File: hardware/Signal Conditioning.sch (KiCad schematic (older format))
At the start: 16 parts, among them U2 LM2902N

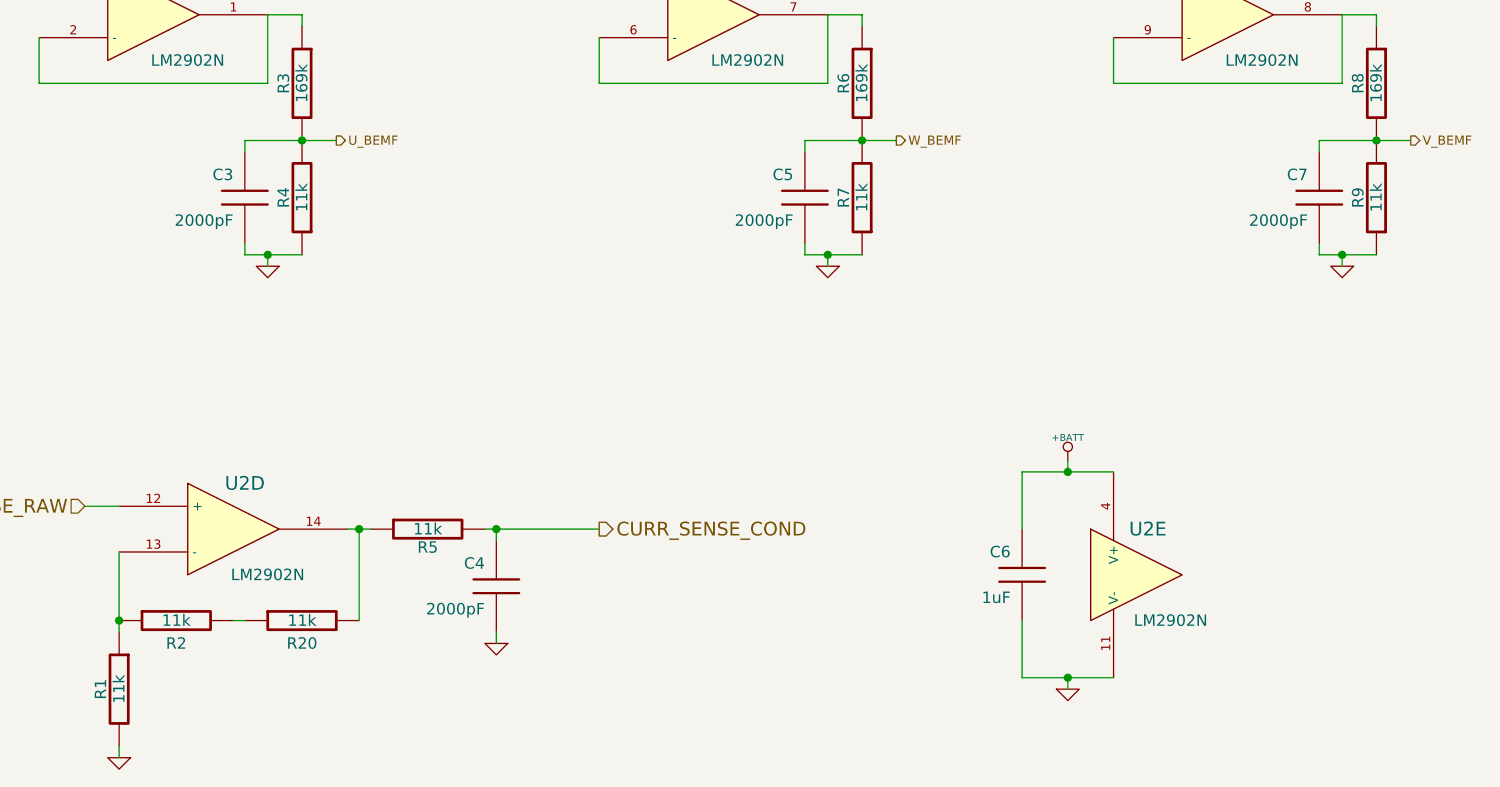
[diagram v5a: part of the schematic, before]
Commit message: Fixed item properties and generated a BOM.
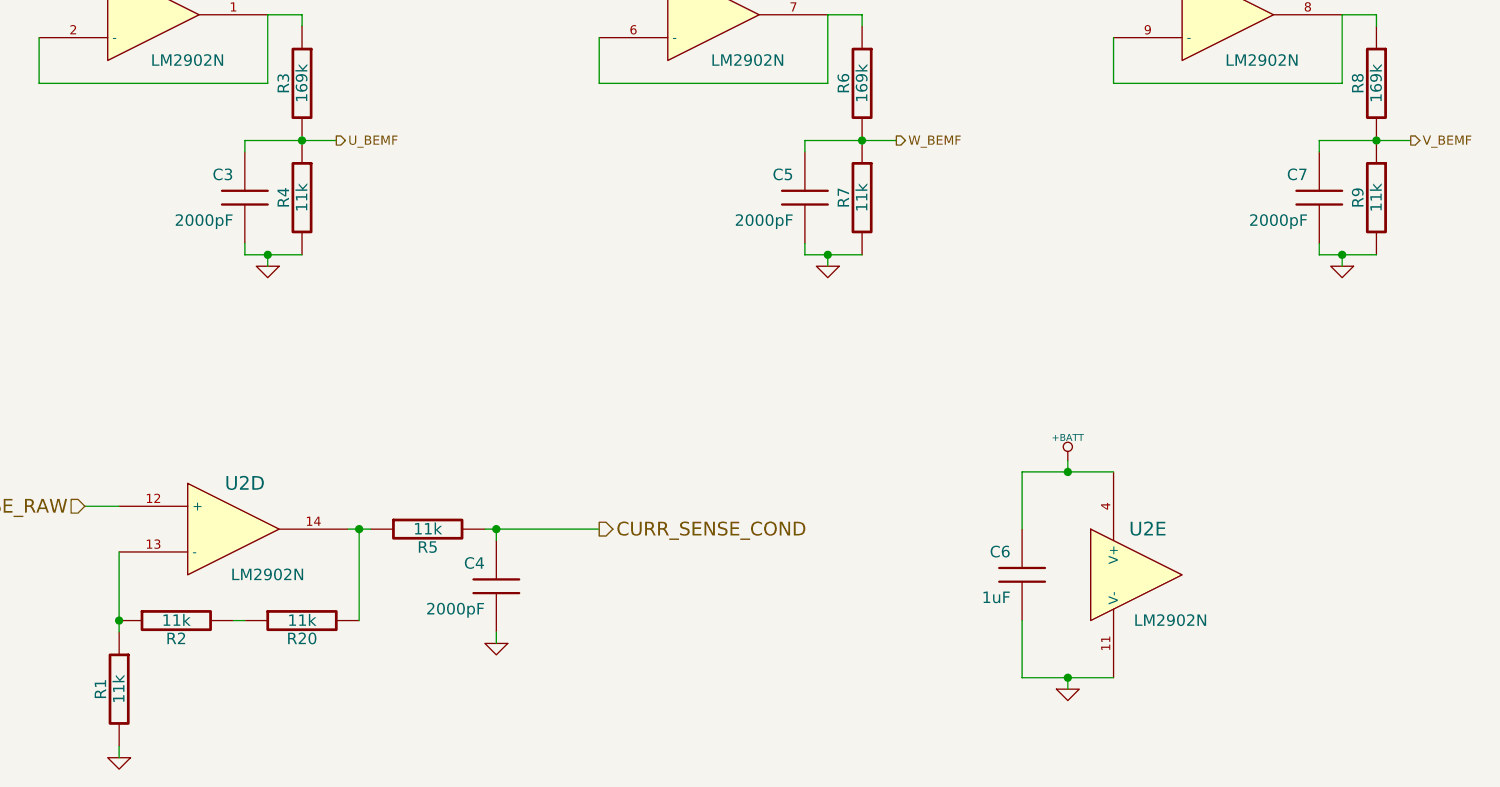
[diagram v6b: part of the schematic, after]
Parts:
- R1, R5: Digikey P/N 7.15KXBK-ND -> 11.0KXBK-ND; Mfg P/N MFR-25FBF52-7K15 -> MFR-25FBF52-11K; Mouser P/N 603-MFR-25FBF52-7K15 -> 603-MFR-25FBF52-11K
- R2, R20: Digikey P/N 169KXBK-ND -> 11.0KXBK-ND; Mfg P/N MFR-25FBF52-169K -> MFR-25FBF52-11K; Mouser P/N 603-MFR-25FBF52-169K -> 603-MFR-25FBF52-11K
- U2: Digikey P/N (none) -> LM2902NFS-ND; Mfg P/N (none) -> LM2902N; Mouser P/N (none) -> 512-LM2902N
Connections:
- net GND: now also R4.2, R7.2, R9.2; no longer R4.1, R7.1, R9.1
- net U_BEMF: now also R4.1; no longer R4.2
- net V_BEMF: now also R9.1; no longer R9.2
- net W_BEMF: now also R7.1; no longer R7.2
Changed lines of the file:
@@
-EESchema Schematic File Version 2  date Sun 14 Jun 2015 10:56:58 MST
+EESchema Schematic File Version 2  date Sun 14 Jun 2015 15:22:49 MST
 LIBS:power
 LIBS:device
@@
 Comment4 ""
 $EndDescr
+$Comp
+L R R5
+U 1 1 557DF4C5
+P 4350 4550
+F 0 "R5" V 4430 4550 50  0000 C CNN
+F 1 "11k" V 4350 4550 50  0000 C CNN
+F 4 "MFR-25FBF52-11K" V 4350 4550 60  0001 C CNN "Mfg P/N"
+F 5 "11.0KXBK-ND" V 4350 4550 60  0001 C CNN "Digikey P/N"
+F 6 "603-MFR-25FBF52-11K" V 4350 4550 60  0001 C CNN "Mouser P/N"
+	1    4350 4550
+	0    -1   1    0
+$EndComp
+$Comp
+L R R9
+U 1 1 557DF4AD
+P 8500 3100
+F 0 "R9" V 8580 3100 50  0000 C CNN
+F 1 "11k" V 8500 3100 50  0000 C CNN
+F 4 "MFR-25FBF52-11K" V 8500 3100 60  0001 C CNN "Mfg P/N"
+F 5 "11.0KXBK-ND" V 8500 3100 60  0001 C CNN "Digikey P/N"
+F 6 "603-MFR-25FBF52-11K" V 8500 3100 60  0001 C CNN "Mouser P/N"
+	1    8500 3100
+	-1   0    0    -1
+$EndComp
+$Comp
+L R R7
+U 1 1 557DF4A0
+P 6250 3100
+F 0 "R7" V 6330 3100 50  0000 C CNN
+F 1 "11k" V 6250 3100 50  0000 C CNN
+F 4 "MFR-25FBF52-11K" V 6250 3100 60  0001 C CNN "Mfg P/N"
+F 5 "11.0KXBK-ND" V 6250 3100 60  0001 C CNN "Digikey P/N"
+F 6 "603-MFR-25FBF52-11K" V 6250 3100 60  0001 C CNN "Mouser P/N"
+	1    6250 3100
+	-1   0    0    -1
+$EndComp
+$Comp
+L R R4
+U 1 1 557DF493
+P 3800 3100
+F 0 "R4" V 3880 3100 50  0000 C CNN
+F 1 "11k" V 3800 3100 50  0000 C CNN
+F 4 "MFR-25FBF52-11K" V 3800 3100 60  0001 C CNN "Mfg P/N"
+F 5 "11.0KXBK-ND" V 3800 3100 60  0001 C CNN "Digikey P/N"
+F 6 "603-MFR-25FBF52-11K" V 3800 3100 60  0001 C CNN "Mouser P/N"
+	1    3800 3100
+	-1   0    0    -1
+$EndComp
+$Comp
+L R R20
+U 1 1 557DF485
+P 3800 4950
+F 0 "R20" V 3880 4950 50  0000 C CNN
+F 1 "11k" V 3800 4950 50  0000 C CNN
+F 4 "MFR-25FBF52-11K" V 3800 4950 60  0001 C CNN "Mfg P/N"
+F 5 "11.0KXBK-ND" V 3800 4950 60  0001 C CNN "Digikey P/N"
+F 6 "603-MFR-25FBF52-11K" V 3800 4950 60  0001 C CNN "Mouser P/N"
+	1    3800 4950
+	0    -1   1    0
+$EndComp
+$Comp
+L R R2
+U 1 1 557DF477
+P 3250 4950
+F 0 "R2" V 3330 4950 50  0000 C CNN
+F 1 "11k" V 3250 4950 50  0000 C CNN
+F 4 "MFR-25FBF52-11K" V 3250 4950 60  0001 C CNN "Mfg P/N"
+F 5 "11.0KXBK-ND" V 3250 4950 60  0001 C CNN "Digikey P/N"
+F 6 "603-MFR-25FBF52-11K" V 3250 4950 60  0001 C CNN "Mouser P/N"
+	1    3250 4950
+	0    -1   1    0
+$EndComp
 Wire Wire Line
 	3550 4950 3500 4950
@@
 Connection ~ 7150 4300
 $Comp
-L R R2
-U 1 1 555D645C
-P 3250 4950
-F 0 "R2" V 3350 4950 50  0000 C CNN
-F 1 "11k" V 3250 4950 50  0000 C CNN
-F 4 "MFR-25FBF52-169K" V 3250 4950 60  0001 C CNN "Mfg P/N"
-F 5 "169KXBK-ND" V 3250 4950 60  0001 C CNN "Digikey P/N"
-F 6 "603-MFR-25FBF52-169K" V 3250 4950 60  0001 C CNN "Mouser P/N"
-	1    3250 4950
-	0    -1   1    0
-$EndComp
-$Comp
-L R R20
-U 1 1 555D6392
-P 3800 4950
-F 0 "R20" V 3900 4950 50  0000 C CNN
-F 1 "11k" V 3800 4950 50  0000 C CNN
-F 4 "MFR-25FBF52-169K" V 3800 4950 60  0001 C CNN "Mfg P/N"
-F 5 "169KXBK-ND" V 3800 4950 60  0001 C CNN "Digikey P/N"
-F 6 "603-MFR-25FBF52-169K" V 3800 4950 60  0001 C CNN "Mouser P/N"
-	1    3800 4950
-	0    -1   1    0
-$EndComp
-$Comp
-L +BATT #PWR08
+L +BATT #PWR10
 U 1 1 555D62EA
 P 7150 4250
-F 0 "#PWR08" H 7150 4200 20  0001 C CNN
+F 0 "#PWR10" H 7150 4200 20  0001 C CNN
 F 1 "+BATT" H 7150 4350 30  0000 C CNN
 	1    7150 4250
@@
 $EndComp
 $Comp
-L GND #PWR09
+L GND #PWR11
 U 1 1 555D62D6
 P 7150 5250
-F 0 "#PWR09" H 7150 5250 30  0001 C CNN
+F 0 "#PWR11" H 7150 5250 30  0001 C CNN
 F 1 "GND" H 7150 5180 30  0001 C CNN
 	1    7150 5250
@@
 F 0 "R1" V 3080 5250 50  0000 C CNN
 F 1 "11k" V 3000 5250 50  0000 C CNN
-F 4 "MFR-25FBF52-7K15" V 3000 5250 60  0001 C CNN "Mfg P/N"
-F 5 "7.15KXBK-ND" V 3000 5250 60  0001 C CNN "Digikey P/N"
-F 6 "603-MFR-25FBF52-7K15" V 3000 5250 60  0001 C CNN "Mouser P/N"
+F 4 "MFR-25FBF52-11K" V 3000 5250 60  0001 C CNN "Mfg P/N"
+F 5 "11.0KXBK-ND" V 3000 5250 60  0001 C CNN "Digikey P/N"
+F 6 "603-MFR-25FBF52-11K" V 3000 5250 60  0001 C CNN "Mouser P/N"
 	1    3000 5250
 	-1   0    0    -1
@@
 $EndComp
 $Comp
-L R R9
-U 1 1 555D5374
-P 8500 3100
-F 0 "R9" V 8580 3100 50  0000 C CNN
-F 1 "11k" V 8500 3100 50  0000 C CNN
-F 4 "MFR-25FBF52-11K" V 8500 3100 60  0001 C CNN "Mfg P/N"
-F 5 "11.0KXBK-ND" V 8500 3100 60  0001 C CNN "Digikey P/N"
-F 6 "603-MFR-25FBF52-11K" V 8500 3100 60  0001 C CNN "Mouser P/N"
-	1    8500 3100
-	-1   0    0    1
-$EndComp
-$Comp
-L R R7
-U 1 1 555D5371
-P 6250 3100
-F 0 "R7" V 6330 3100 50  0000 C CNN
-F 1 "11k" V 6250 3100 50  0000 C CNN
-F 4 "MFR-25FBF52-11K" V 6250 3100 60  0001 C CNN "Mfg P/N"
-F 5 "11.0KXBK-ND" V 6250 3100 60  0001 C CNN "Digikey P/N"
-F 6 "603-MFR-25FBF52-11K" V 6250 3100 60  0001 C CNN "Mouser P/N"
-	1    6250 3100
-	-1   0    0    1
-$EndComp
-$Comp
-L R R4
-U 1 1 555D5368
-P 3800 3100
-F 0 "R4" V 3880 3100 50  0000 C CNN
-F 1 "11k" V 3800 3100 50  0000 C CNN
-F 4 "MFR-25FBF52-11K" V 3800 3100 60  0001 C CNN "Mfg P/N"
-F 5 "11.0KXBK-ND" V 3800 3100 60  0001 C CNN "Digikey P/N"
-F 6 "603-MFR-25FBF52-11K" V 3800 3100 60  0001 C CNN "Mouser P/N"
-	1    3800 3100
-	-1   0    0    1
-$EndComp
-$Comp
 L C C6
 U 1 1 555D4FE1
@@
 $EndComp
 $Comp
-L GND #PWR010
+L GND #PWR8
 U 1 1 554659C8
 P 4650 5050
-F 0 "#PWR010" H 4650 5050 30  0001 C CNN
+F 0 "#PWR8" H 4650 5050 30  0001 C CNN
 F 1 "GND" H 4650 4980 30  0001 C CNN
 	1    4650 5050
@@
 $EndComp
 $Comp
-L R R5
-U 1 1 554659A9
-P 4350 4550
-F 0 "R5" V 4430 4550 50  0000 C CNN
-F 1 "11k" V 4350 4550 50  0000 C CNN
-F 4 "MFR-25FBF52-7K15" V 4350 4550 60  0001 C CNN "Mfg P/N"
-F 5 "7.15KXBK-ND" V 4350 4550 60  0001 C CNN "Digikey P/N"
-F 6 "603-MFR-25FBF52-7K15" V 4350 4550 60  0001 C CNN "Mouser P/N"
-	1    4350 4550
-	0    -1   1    0
-$EndComp
-$Comp
-L GND #PWR011
+L GND #PWR6
 U 1 1 5546596B
 P 3000 5550
-F 0 "#PWR011" H 3000 5550 30  0001 C CNN
+F 0 "#PWR6" H 3000 5550 30  0001 C CNN
 F 1 "GND" H 3000 5480 30  0001 C CNN
 	1    3000 5550
@@
 F 0 "U2" H 3200 2500 60  0000 C CNN
 F 1 "LM2902N" H 3300 2100 50  0000 C CNN
+F 3 "datasheets/lm2902.pdf" H 3150 2300 60  0001 C CNN
+F 4 "LM2902N" H 3150 2300 60  0001 C CNN "Mfg P/N"
+F 5 "LM2902NFS-ND" H 3150 2300 60  0001 C CNN "Digikey P/N"
+F 6 "512-LM2902N" H 3150 2300 60  0001 C CNN "Mouser P/N"
 	1    3150 2300
 	1    0    0    -1
@@
 $EndComp
 $Comp
-L GND #PWR012
+L GND #PWR7
 U 1 1 5533F7C4
 P 3650 3400
-F 0 "#PWR012" H 3650 3400 30  0001 C CNN
+F 0 "#PWR7" H 3650 3400 30  0001 C CNN
 F 1 "GND" H 3650 3330 30  0001 C CNN
 	1    3650 3400
@@
 $EndComp
 $Comp
-L GND #PWR013
+L GND #PWR12
 U 1 1 5533F7C3
 P 8350 3400
-F 0 "#PWR013" H 8350 3400 30  0001 C CNN
+F 0 "#PWR12" H 8350 3400 30  0001 C CNN
 F 1 "GND" H 8350 3330 30  0001 C CNN
 	1    8350 3400
@@
 $EndComp
 $Comp
-L GND #PWR014
+L GND #PWR9
 U 1 1 5533F7BA
 P 6100 3400
-F 0 "#PWR014" H 6100 3400 30  0001 C CNN
+F 0 "#PWR9" H 6100 3400 30  0001 C CNN
 F 1 "GND" H 6100 3330 30  0001 C CNN
 	1    6100 3400
